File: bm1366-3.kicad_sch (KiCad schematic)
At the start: 76 parts, among them U14 BM1366_mode1, U26 ADP171AUJ-R7, U27 ADP171AUJ-R7, U28 TLV3544

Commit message: Resolved all unconnected pins, re-annotated, reviewed for layout
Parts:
- removed R6 (x4): 33, Resistor_SMD:R_0402_1005Metric, symbol Device:R_US
- added TP13 (x9): TestPoint, TestPoint:TestPoint_Pad_D1.5mm, symbol Connector:TestPoint
- renumbered U26 to U25, U27 to U26
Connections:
- net CLKO: now also U14.21 (CLKO), TP13.1
- net CO: now also U14.20 (CO), TP13.1
- net NRSTO: now also U14.24 (NRSTO), TP13.1
- net RI: now also U14.22 (RI), TP13.1
- net TEMP_N1: now also TP13.1
- net TEMP_N2: now also TP13.1
- net TEMP_P1: now also TP13.1
- net TEMP_P2: now also TP13.1
- net BO: now reaches U14.23 (BO)
- net BO: now also TP13.1
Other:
- note added: "OPAMP Bypass"

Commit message: Rough parts placement
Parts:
- TP13: footprint TestPoint:TestPoint_Pad_D1.5mm -> TestPoint:TestPoint_Pad_D1.0mm
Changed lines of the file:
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@@
     (effects (font (size 1.27 1.27)) (justify left bottom))
   )
-  (label "-VDD" (at 259.715 33.02 180) (fields_autoplaced)
+  (label "-VDD3" (at 259.715 33.02 180) (fields_autoplaced)
     (effects (font (size 1.27 1.27)) (justify right bottom))
   )
@@
     (effects (font (size 1.27 1.27)) (justify left bottom))
   )
-  (label "-VDD" (at 53.34 51.435 180) (fields_autoplaced)
+  (label "-VDD3" (at 53.34 51.435 180) (fields_autoplaced)
     (effects (font (size 1.27 1.27)) (justify right bottom))
   )
@@
     (effects (font (size 1.27 1.27)) (justify left bottom))
   )
-  (label "VDD" (at 52.705 33.655 180) (fields_autoplaced)
+  (label "VDD3" (at 52.705 33.655 180) (fields_autoplaced)
     (effects (font (size 1.27 1.27)) (justify right bottom))
   )
@@
     (effects (font (size 1.27 1.27)) (justify left bottom))
   )
-  (label "VDD" (at 16.51 45.085 0) (fields_autoplaced)
+  (label "VDD3" (at 16.51 45.085 0) (fields_autoplaced)
     (effects (font (size 1.27 1.27)) (justify left bottom))
   )
@@
     (effects (font (size 1.27 1.27)) (justify left bottom))
   )
-  (label "VDD" (at 132.08 45.085 0) (fields_autoplaced)
+  (label "VDD3" (at 132.08 45.085 0) (fields_autoplaced)
     (effects (font (size 1.27 1.27)) (justify left bottom))
   )
@@
     (effects (font (size 1.27 1.27)) (justify left bottom))
   )
-  (label "-VDD" (at 116.205 131.445 0) (fields_autoplaced)
+  (label "-VDD3" (at 116.205 131.445 0) (fields_autoplaced)
     (effects (font (size 1.27 1.27)) (justify left bottom))
   )
-  (label "VDD" (at 72.39 45.085 0) (fields_autoplaced)
+  (label "VDD3" (at 72.39 45.085 0) (fields_autoplaced)
     (effects (font (size 1.27 1.27)) (justify left bottom))
   )
@@
     (effects (font (size 1.27 1.27)) (justify left bottom))
   )
-  (label "VDD" (at 153.035 144.145 0) (fields_autoplaced)
+  (label "VDD3" (at 153.035 144.145 0) (fields_autoplaced)
     (effects (font (size 1.27 1.27)) (justify left bottom))
   )
@@
     (effects (font (size 1.27 1.27)) (justify left bottom))
   )
-  (label "-VDD" (at 188.595 45.085 0) (fields_autoplaced)
+  (label "-VDD3" (at 188.595 45.085 0) (fields_autoplaced)
     (effects (font (size 1.27 1.27)) (justify left bottom))
   )
-  (label "VDD" (at 203.835 62.865 0) (fields_autoplaced)
+  (label "VDD3" (at 203.835 62.865 0) (fields_autoplaced)
     (effects (font (size 1.27 1.27)) (justify left bottom))
   )
@@
     (effects (font (size 1.27 1.27)) (justify left bottom))
   )
-  (label "VDD" (at 240.665 17.78 0) (fields_autoplaced)
+  (label "VDD3" (at 240.665 17.78 0) (fields_autoplaced)
     (effects (font (size 1.27 1.27)) (justify left bottom))
   )
-  (label "VDD" (at 75.565 62.865 0) (fields_autoplaced)
+  (label "VDD3" (at 75.565 62.865 0) (fields_autoplaced)
     (effects (font (size 1.27 1.27)) (justify left bottom))
   )
@@
       (effects (font (size 1.27 1.27)) (justify left) hide)
     )
-    (property "Footprint" "TestPoint:TestPoint_Pad_D1.5mm" (at 175.26 99.695 0)
+    (property "Footprint" "TestPoint:TestPoint_Pad_D1.0mm" (at 175.26 99.695 0)
       (effects (font (size 1.27 1.27)) hide)
     )
@@
       (effects (font (size 1.27 1.27)) (justify left) hide)
     )
-    (property "Footprint" "TestPoint:TestPoint_Pad_D1.5mm" (at 120.65 139.065 0)
+    (property "Footprint" "TestPoint:TestPoint_Pad_D1.0mm" (at 120.65 139.065 0)
       (effects (font (size 1.27 1.27)) hide)
     )
@@
       (effects (font (size 1.27 1.27)) (justify left) hide)
     )
-    (property "Footprint" "TestPoint:TestPoint_Pad_D1.5mm" (at 42.545 102.235 0)
+    (property "Footprint" "TestPoint:TestPoint_Pad_D1.0mm" (at 42.545 102.235 0)
       (effects (font (size 1.27 1.27)) hide)
     )
@@
       (effects (font (size 1.27 1.27)) (justify left) hide)
     )
-    (property "Footprint" "TestPoint:TestPoint_Pad_D1.5mm" (at 42.545 99.695 0)
+    (property "Footprint" "TestPoint:TestPoint_Pad_D1.0mm" (at 42.545 99.695 0)
       (effects (font (size 1.27 1.27)) hide)
     )
@@
       (effects (font (size 1.27 1.27)) (justify left) hide)
     )
-    (property "Footprint" "TestPoint:TestPoint_Pad_D1.5mm" (at 120.65 172.085 0)
+    (property "Footprint" "TestPoint:TestPoint_Pad_D1.0mm" (at 120.65 172.085 0)
       (effects (font (size 1.27 1.27)) hide)
     )
@@
       (effects (font (size 1.27 1.27)) (justify left) hide)
     )
-    (property "Footprint" "TestPoint:TestPoint_Pad_D1.5mm" (at 175.26 102.235 0)
+    (property "Footprint" "TestPoint:TestPoint_Pad_D1.0mm" (at 175.26 102.235 0)
       (effects (font (size 1.27 1.27)) hide)
     )

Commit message: more parts placement
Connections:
- net BI: no longer C8.2, R6.1, U14.6 (BI), U28.8
- net CI: no longer C8.2, R6.1, U14.9 (CI), U28.1
- net GND3: no longer R6.2, R6.2, R6.2, R6.2
- net NRSTI: no longer C8.2, R6.1, U14.5 (NRSTI), U28.7
- net RO: no longer R6.1, U14.7 (RO)
- net BO renamed BO3
- net CLKO renamed CLKO3
- net CO renamed CO3
- net NRSTO renamed NRSTO3
- net RI renamed RI3
- net TEMP_N1 renamed TEMP_N1_3
- net TEMP_N2 renamed TEMP_N2_3
- net TEMP_P1 renamed TEMP_P1_3
- net TEMP_P2 renamed TEMP_P2_3
- new net BI3: C8.2, R6.1, U14.6 (BI), U28.8
- new net CI3: C8.2, R6.1, U14.9 (CI), U28.1
- new net GND: R6.2, R6.2, R6.2, R6.2
- new net NRSTI3: C8.2, R6.1, U14.5 (NRSTI), U28.7
- new net RO3: R6.1, U14.7 (RO)
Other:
- moved on the sheet: TP13
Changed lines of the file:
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@@
     (stroke (width 0) (type default))
   )
-  (wire (pts (xy 175.26 97.155) (xy 184.15 97.155))
-    (stroke (width 0) (type default))
-  )
   (wire (pts (xy 175.895 118.745) (xy 175.895 123.825))
     (stroke (width 0) (type default))
@@
     (stroke (width 0) (type default))
   )
+  (wire (pts (xy 171.45 94.615) (xy 184.15 94.615))
+    (stroke (width 0) (type default))
+  )
   (wire (pts (xy 250.19 76.835) (xy 250.19 62.865))
     (stroke (width 0) (type default))
@@
     (stroke (width 0) (type default))
   )
-  (wire (pts (xy 175.26 94.615) (xy 184.15 94.615))
-    (stroke (width 0) (type default))
-  )
   (wire (pts (xy 153.035 45.085) (xy 154.94 45.085))
     (stroke (width 0) (type default))
@@
     (stroke (width 0) (type default))
   )
+  (wire (pts (xy 171.45 97.155) (xy 184.15 97.155))
+    (stroke (width 0) (type default))
+  )
   (wire (pts (xy 91.44 84.455) (xy 146.05 84.455))
     (stroke (width 0) (type default))
@@
     (effects (font (size 1.27 1.27)) (justify left bottom))
   )
-  (label "TEMP_N2" (at 182.88 97.155 180) (fields_autoplaced)
+  (label "TEMP_N2_3" (at 181.61 97.155 180) (fields_autoplaced)
     (effects (font (size 1.27 1.27)) (justify right bottom))
   )
-  (label "TEMP_P1" (at 42.545 94.615 0) (fields_autoplaced)
+  (label "TEMP_P1_3" (at 42.545 94.615 0) (fields_autoplaced)
     (effects (font (size 1.27 1.27)) (justify left bottom))
   )
-  (label "NRSTI" (at 124.46 42.545 180) (fields_autoplaced)
+  (label "NRSTI3" (at 124.46 42.545 180) (fields_autoplaced)
     (effects (font (size 1.27 1.27)) (justify right bottom))
   )
@@
     (effects (font (size 1.27 1.27)) (justify left bottom))
   )
-  (label "-VDD3" (at 259.715 33.02 180) (fields_autoplaced)
+  (label "GND2" (at 259.715 33.02 180) (fields_autoplaced)
     (effects (font (size 1.27 1.27)) (justify right bottom))
   )
-  (label "RO" (at 188.595 50.165 0) (fields_autoplaced)
+  (label "RO3" (at 188.595 50.165 0) (fields_autoplaced)
     (effects (font (size 1.27 1.27)) (justify left bottom))
   )
-  (label "-VDD3" (at 53.34 51.435 180) (fields_autoplaced)
+  (label "GND2" (at 53.34 51.435 180) (fields_autoplaced)
     (effects (font (size 1.27 1.27)) (justify right bottom))
   )
-  (label "TEMP_P2" (at 182.88 94.615 180) (fields_autoplaced)
+  (label "TEMP_P2_3" (at 181.61 94.615 180) (fields_autoplaced)
     (effects (font (size 1.27 1.27)) (justify right bottom))
   )
@@
     (effects (font (size 1.27 1.27)) (justify left bottom))
   )
-  (label "NRSTI" (at 31.75 81.915 0) (fields_autoplaced)
+  (label "NRSTI3" (at 31.75 81.915 0) (fields_autoplaced)
     (effects (font (size 1.27 1.27)) (justify left bottom))
   )
-  (label "CLKO" (at 222.885 89.535 0) (fields_autoplaced)
+  (label "CLKO3" (at 222.885 89.535 0) (fields_autoplaced)
     (effects (font (size 1.27 1.27)) (justify left bottom))
   )
-  (label "TEMP_N1" (at 42.545 97.155 0) (fields_autoplaced)
+  (label "TEMP_N1_3" (at 42.545 97.155 0) (fields_autoplaced)
     (effects (font (size 1.27 1.27)) (justify left bottom))
   )
-  (label "CI" (at 31.75 92.075 0) (fields_autoplaced)
+  (label "CI3" (at 31.75 92.075 0) (fields_autoplaced)
     (effects (font (size 1.27 1.27)) (justify left bottom))
   )
@@
     (effects (font (size 1.27 1.27)) (justify right bottom))
   )
-  (label "CO" (at 222.885 92.075 0) (fields_autoplaced)
+  (label "CO3" (at 222.885 92.075 0) (fields_autoplaced)
     (effects (font (size 1.27 1.27)) (justify left bottom))
   )
@@
     (effects (font (size 1.27 1.27)) (justify left bottom))
   )
-  (label "GND" (at 77.47 123.825 0) (fields_autoplaced)
+  (label "GND3" (at 77.47 123.825 0) (fields_autoplaced)
     (effects (font (size 1.27 1.27)) (justify left bottom))
   )
-  (label "RO" (at 31.75 86.995 0) (fields_autoplaced)
+  (label "RO3" (at 31.75 86.995 0) (fields_autoplaced)
     (effects (font (size 1.27 1.27)) (justify left bottom))
   )
@@
     (effects (font (size 1.27 1.27)) (justify left bottom))
   )
-  (label "GND" (at 86.995 195.58 0) (fields_autoplaced)
+  (label "GND3" (at 86.995 195.58 0) (fields_autoplaced)
     (effects (font (size 1.27 1.27)) (justify left bottom))
   )
@@
     (effects (font (size 1.27 1.27)) (justify left bottom))
   )
-  (label "RI" (at 222.885 86.995 0) (fields_autoplaced)
+  (label "CLKI3" (at 32.385 89.535 0) (fields_autoplaced)
+    (effects (font (size 1.27 1.27)) (justify left bottom))
+  )
+  (label "RI3" (at 222.885 86.995 0) (fields_autoplaced)
     (effects (font (size 1.27 1.27)) (justify left bottom))
   )
-  (label "GND" (at 153.035 156.21 0) (fields_autoplaced)
+  (label "GND3" (at 153.035 156.21 0) (fields_autoplaced)
     (effects (font (size 1.27 1.27)) (justify left bottom))
   )
@@
     (effects (font (size 1.27 1.27)) (justify left bottom))
   )
-  (label "-VDD3" (at 116.205 131.445 0) (fields_autoplaced)
+  (label "GND2" (at 116.205 131.445 0) (fields_autoplaced)
     (effects (font (size 1.27 1.27)) (justify left bottom))
   )
@@
     (effects (font (size 1.27 1.27)) (justify left bottom))
   )
-  (label "BI" (at 181.61 42.545 180) (fields_autoplaced)
+  (label "BI3" (at 181.61 42.545 180) (fields_autoplaced)
     (effects (font (size 1.27 1.27)) (justify right bottom))
   )
-  (label "BI" (at 31.75 84.455 0) (fields_autoplaced)
+  (label "BI3" (at 31.75 84.455 0) (fields_autoplaced)
     (effects (font (size 1.27 1.27)) (justify left bottom))
   )
@@
     (effects (font (size 1.27 1.27)) (justify left bottom))
   )
-  (label "GND" (at 205.74 123.825 0) (fields_autoplaced)
+  (label "GND3" (at 205.74 123.825 0) (fields_autoplaced)
     (effects (font (size 1.27 1.27)) (justify left bottom))
   )
-  (label "BO" (at 222.885 84.455 0) (fields_autoplaced)
+  (label "BO3" (at 222.885 84.455 0) (fields_autoplaced)
     (effects (font (size 1.27 1.27)) (justify left bottom))
   )
-  (label "CI" (at 65.405 42.545 180) (fields_autoplaced)
+  (label "CI3" (at 65.405 42.545 180) (fields_autoplaced)
     (effects (font (size 1.27 1.27)) (justify right bottom))
   )
@@
     (effects (font (size 1.27 1.27)) (justify left bottom))
   )
-  (label "GND" (at 86.995 162.56 0) (fields_autoplaced)
+  (label "GND3" (at 86.995 162.56 0) (fields_autoplaced)
     (effects (font (size 1.27 1.27)) (justify left bottom))
   )
-  (label "NRSTO" (at 222.885 81.915 0) (fields_autoplaced)
+  (label "NRSTO3" (at 222.885 81.915 0) (fields_autoplaced)
     (effects (font (size 1.27 1.27)) (justify left bottom))
   )
@@
     )
   )
-  (symbol (lib_id "Connector:TestPoint") (at 175.26 94.615 90) (mirror x) (unit 1)
+  (symbol (lib_id "Connector:TestPoint") (at 171.45 94.615 90) (mirror x) (unit 1)
     (in_bom no) (on_board yes) (dnp no)
-    (property "Reference" "TP13" (at 168.91 94.615 90)
+    (property "Reference" "TP13" (at 165.1 94.615 90)
       (effects (font (size 1.27 1.27)))
     )
-    (property "Value" "TestPoint" (at 169.545 95.8849 90)
+    (property "Value" "TestPoint" (at 165.735 95.8849 90)
       (effects (font (size 1.27 1.27)) (justify left) hide)
     )
-    (property "Footprint" "TestPoint:TestPoint_Pad_D1.0mm" (at 175.26 99.695 0)
+    (property "Footprint" "TestPoint:TestPoint_Pad_D1.0mm" (at 171.45 99.695 0)
       (effects (font (size 1.27 1.27)) hide)
     )
-    (property "Datasheet" "~" (at 175.26 99.695 0)
+    (property "Datasheet" "~" (at 171.45 99.695 0)
       (effects (font (size 1.27 1.27)) hide)
     )
@@
     )
   )
-  (symbol (lib_id "Connector:TestPoint") (at 175.26 97.155 90) (mirror x) (unit 1)
+  (symbol (lib_id "Connector:TestPoint") (at 171.45 97.155 90) (mirror x) (unit 1)
     (in_bom no) (on_board yes) (dnp no)
-    (property "Reference" "TP13" (at 168.91 97.155 90)
+    (property "Reference" "TP13" (at 165.1 97.155 90)
       (effects (font (size 1.27 1.27)))
     )
-    (property "Value" "TestPoint" (at 169.545 98.4249 90)
+    (property "Value" "TestPoint" (at 165.735 98.4249 90)
       (effects (font (size 1.27 1.27)) (justify left) hide)
     )
-    (property "Footprint" "TestPoint:TestPoint_Pad_D1.0mm" (at 175.26 102.235 0)
+    (property "Footprint" "TestPoint:TestPoint_Pad_D1.0mm" (at 171.45 102.235 0)
       (effects (font (size 1.27 1.27)) hide)
     )
-    (property "Datasheet" "~" (at 175.26 102.235 0)
+    (property "Datasheet" "~" (at 171.45 102.235 0)
       (effects (font (size 1.27 1.27)) hide)
     )

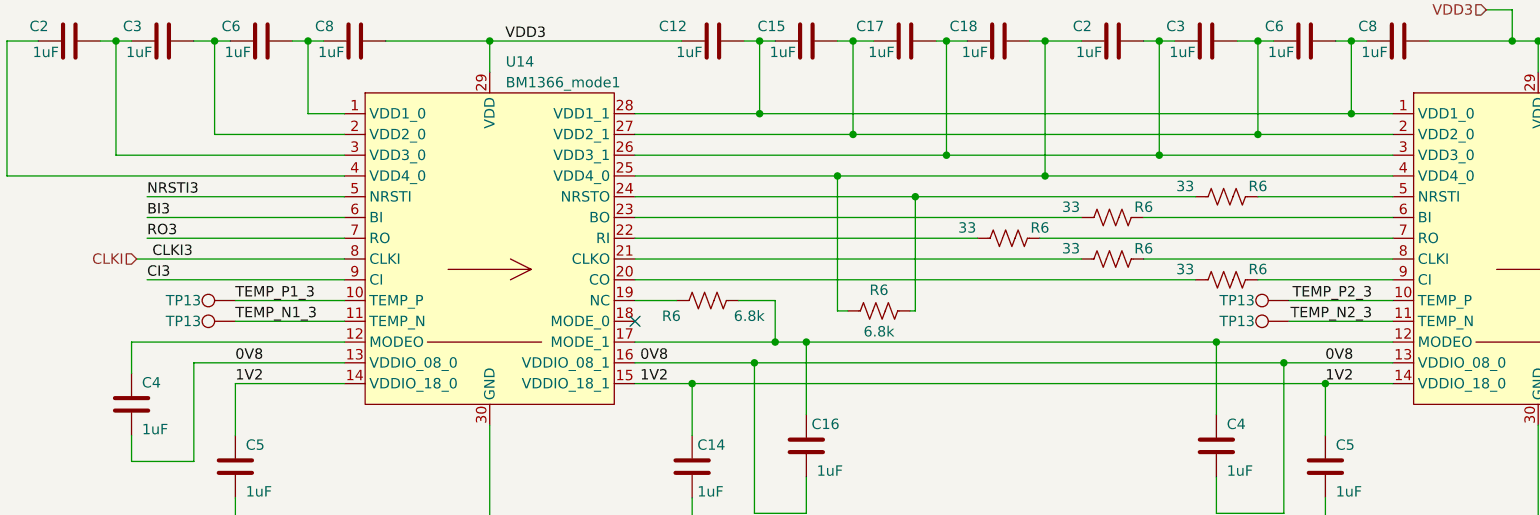
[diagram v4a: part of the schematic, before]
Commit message: shuffle resistors on RI/RO, more routing on ASICs
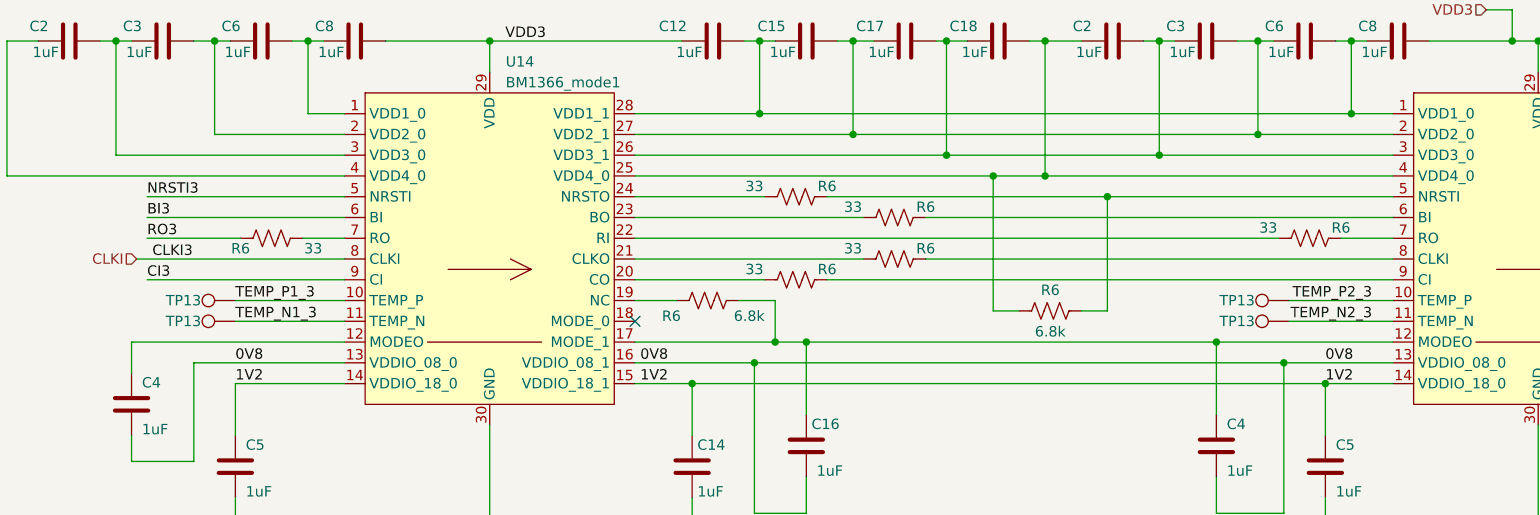
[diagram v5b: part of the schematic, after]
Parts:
- removed R6 (x2): 33, Resistor_SMD:R_0402_1005Metric, symbol Device:R_US
- added R6 (x3): 33, Resistor_SMD:R_0402_1005Metric, symbol Device:R_US
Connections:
- net RO3: now also R6.2; no longer U14.7 (RO)
- net at R6.2: now also U14.5 (NRSTI), R6.2; no longer U14.24 (NRSTO)
- net at U14.20 (CO): now also R6.1
- net at U14.9 (CI): now also R6.2
- new net: R6.1, U14.7 (RO)
- new net: R6.1, U14.24 (NRSTO)
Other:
- moved on the sheet: R6

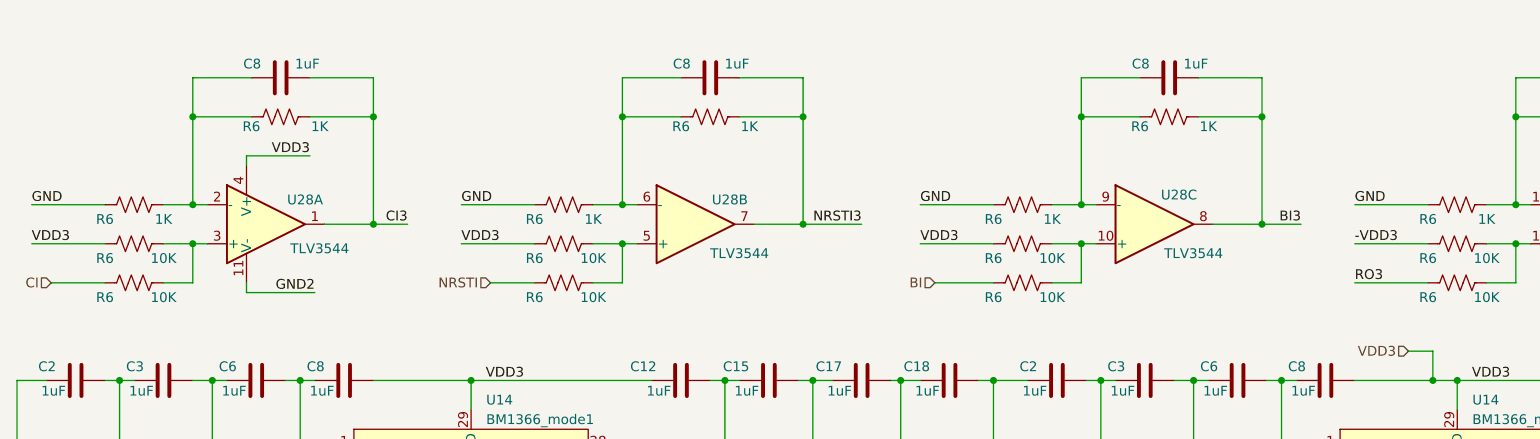
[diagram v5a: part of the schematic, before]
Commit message: finish routing communications
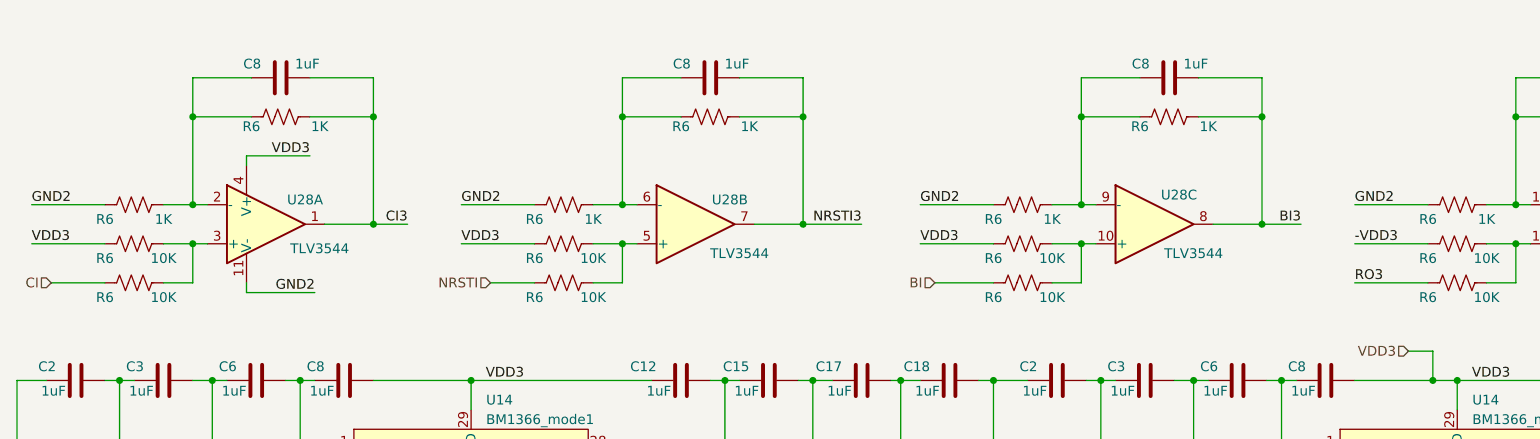
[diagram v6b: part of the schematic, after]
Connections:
- net GND is gone; now on net -VDD3: R6.2, R6.2, R6.2, R6.2
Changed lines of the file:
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@@
     (effects (font (size 1.27 1.27)) (justify left bottom))
   )
-  (label "GND" (at 132.08 40.005 0) (fields_autoplaced)
+  (label "GND2" (at 132.08 40.005 0) (fields_autoplaced)
     (effects (font (size 1.27 1.27)) (justify left bottom))
   )
@@
     (effects (font (size 1.27 1.27)) (justify left bottom))
   )
-  (label "GND" (at 72.39 40.005 0) (fields_autoplaced)
+  (label "GND2" (at 72.39 40.005 0) (fields_autoplaced)
     (effects (font (size 1.27 1.27)) (justify left bottom))
   )
@@
     (effects (font (size 1.27 1.27)) (justify left bottom))
   )
-  (label "GND" (at 16.51 40.005 0) (fields_autoplaced)
+  (label "GND2" (at 16.51 40.005 0) (fields_autoplaced)
     (effects (font (size 1.27 1.27)) (justify left bottom))
   )
@@
     (effects (font (size 1.27 1.27)) (justify left bottom))
   )
-  (label "GND" (at 188.595 40.005 0) (fields_autoplaced)
+  (label "GND2" (at 188.595 40.005 0) (fields_autoplaced)
     (effects (font (size 1.27 1.27)) (justify left bottom))
   )
